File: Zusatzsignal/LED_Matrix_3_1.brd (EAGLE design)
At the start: 15.8 x 21.6 mm, 61 parts, among them IC1 PIC6C595D, X1 SSW-106-02-S-S

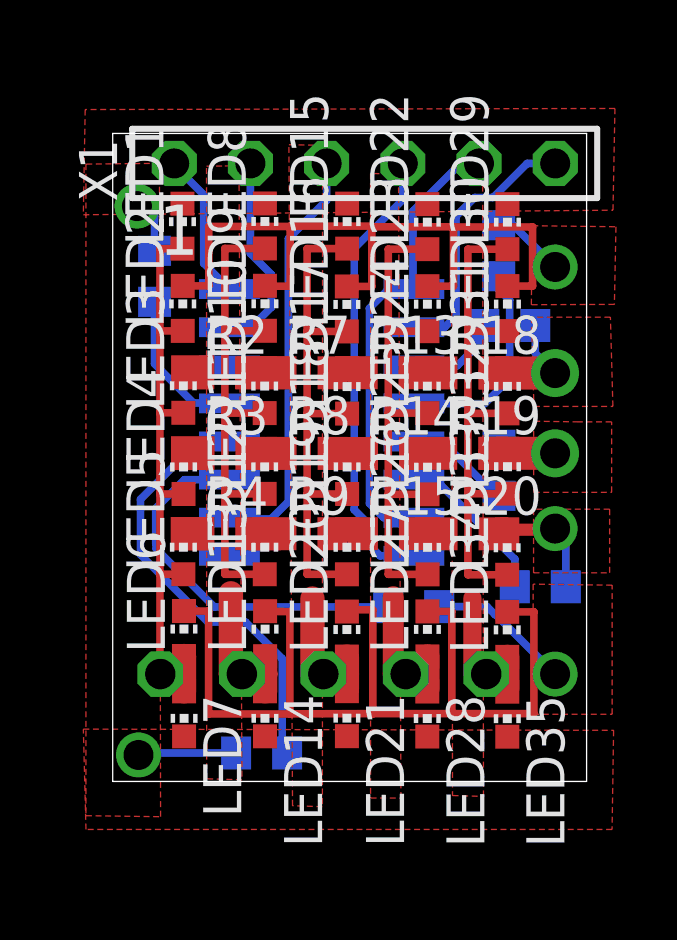
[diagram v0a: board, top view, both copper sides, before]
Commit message: Verbesserung der Zusatzanzeigerplatine
- Änderung des Layouts der Rückseite
- Änderung der Durchführungen auf RM
- Beseitigung von DRC-Fehlern
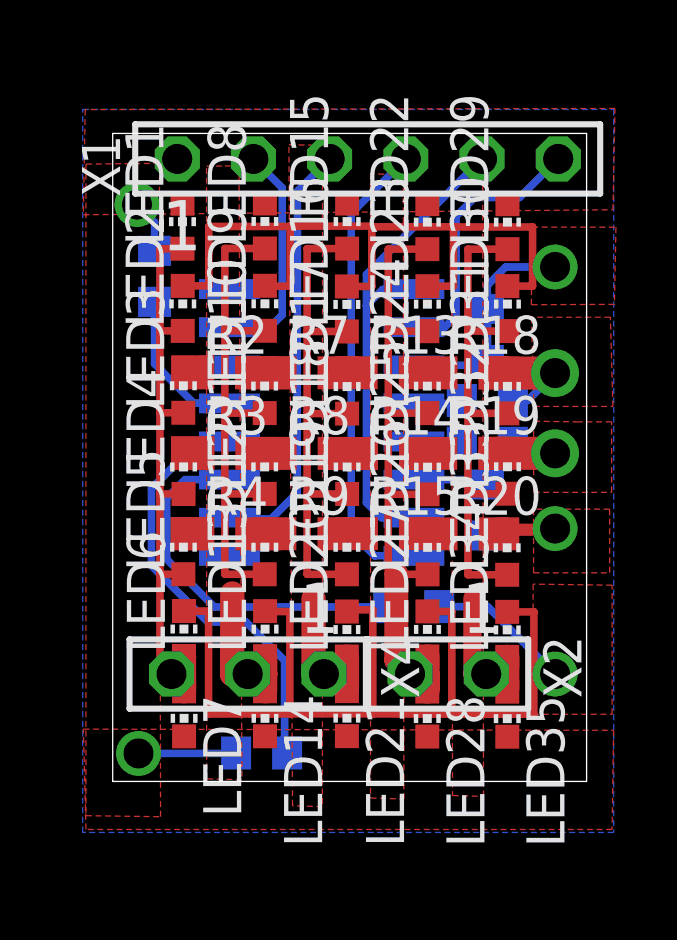
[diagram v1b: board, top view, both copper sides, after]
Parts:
- removed S1, S2, S3, S4, S5: (no value), pinhead:1X01
- added X2: SSW-102-02-S-S, con-samtec:SSW-102-02-S-S
- added X4: SSW-103-02-S-S, con-samtec:SSW-103-02-S-S
- R1, R10, R11, R12, R16, R5, R6: device eagle-ltspice:R0603 -> resistor:R0603
- moved R11 3.11 mm to (12.5, 9.05), turned to 90 degrees
- moved R5 2.81 mm to (12.5, 14.9)
- moved R6 2.61 mm to (12.5, 12.7)
- moved R10 0.98 mm to (12.5, 11.3), turned to 0 degrees
- moved X1 0.18 mm to (8.50, 20.8)
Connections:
- net N$4: now also R6.2; no longer R5.2
- net N$5: now also R5.2; no longer R6.2
- net S1: now also X4.3; no longer S1.1
- net S2: now also X4.2; no longer S2.1
- net S3: now also X4.1; no longer S3.1
- net S4: now also X2.2; no longer S4.1
- net S5: now also X2.1; no longer S5.1
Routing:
- net N$4: track 7.11 -> 1.65 mm
- net GND: track 4.95 -> 0.00 mm
- net N$6: track 5.39 -> 2.56 mm
- net N$7: track 3.59 -> 1.64 mm
- net SCK: track 6.10 -> 7.53 mm
- net VCC: track 15.4 -> 16.8 mm
- net S4: track 22.8 -> 23.7 mm
- net N$5: track 3.16 -> 4.08 mm
- net Z2: track 27.5 -> 28.3 mm
- net Z5: track 3.91 -> 4.44 mm
- added copper zone on layer 16, net GND

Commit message: Optimierung der Zusatzanzeiger & Hauptsignalplatine
- Symmetrischere Auslegung
- Entfernen von MISO/MISO connection zwischen Zusatzanzeiger und Hauptsignalschirm!
-> Zusatzanzeiger-MISO auf Signalschirmplatine nicht mehr connected (NC)
->mögliches Auslesen des DCC-Signals über den MISO-Anschluss (MOSI und SCK für I2C)
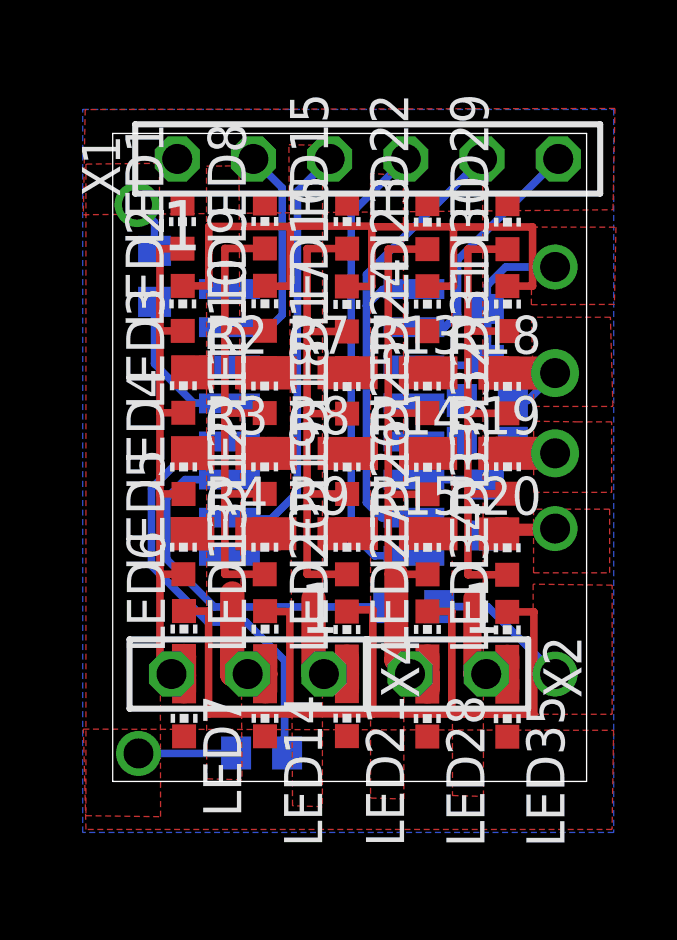
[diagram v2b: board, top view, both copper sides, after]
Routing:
- net DATA: track 9.08 -> 8.20 mm
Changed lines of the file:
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@@
 <layer number="14" name="Route14" color="1" fill="6" visible="no" active="yes"/>
 <layer number="15" name="Route15" color="4" fill="6" visible="no" active="yes"/>
-<layer number="16" name="Bottom" color="1" fill="1" visible="no" active="yes"/>
+<layer number="16" name="Bottom" color="1" fill="1" visible="yes" active="yes"/>
 <layer number="17" name="Pads" color="2" fill="1" visible="yes" active="yes"/>
 <layer number="18" name="Vias" color="2" fill="1" visible="yes" active="yes"/>
@@
 <layer number="20" name="Dimension" color="15" fill="1" visible="yes" active="yes"/>
 <layer number="21" name="tPlace" color="7" fill="1" visible="yes" active="yes"/>
-<layer number="22" name="bPlace" color="7" fill="1" visible="no" active="yes"/>
+<layer number="22" name="bPlace" color="7" fill="1" visible="yes" active="yes"/>
 <layer number="23" name="tOrigins" color="15" fill="1" visible="yes" active="yes"/>
-<layer number="24" name="bOrigins" color="15" fill="1" visible="no" active="yes"/>
+<layer number="24" name="bOrigins" color="15" fill="1" visible="yes" active="yes"/>
 <layer number="25" name="tNames" color="7" fill="1" visible="no" active="yes"/>
 <layer number="26" name="bNames" color="7" fill="1" visible="no" active="yes"/>
@@
 <layer number="38" name="bTest" color="7" fill="1" visible="no" active="yes"/>
 <layer number="39" name="tKeepout" color="4" fill="11" visible="yes" active="yes"/>
-<layer number="40" name="bKeepout" color="1" fill="11" visible="no" active="yes"/>
+<layer number="40" name="bKeepout" color="1" fill="11" visible="yes" active="yes"/>
 <layer number="41" name="tRestrict" color="4" fill="10" visible="yes" active="yes"/>
-<layer number="42" name="bRestrict" color="1" fill="10" visible="no" active="yes"/>
+<layer number="42" name="bRestrict" color="1" fill="10" visible="yes" active="yes"/>
 <layer number="43" name="vRestrict" color="2" fill="10" visible="yes" active="yes"/>
 <layer number="44" name="Drills" color="7" fill="1" visible="no" active="yes"/>
@@
 <layer number="50" name="dxf" color="7" fill="1" visible="no" active="no"/>
 <layer number="51" name="tDocu" color="7" fill="1" visible="yes" active="yes"/>
-<layer number="52" name="bDocu" color="7" fill="1" visible="no" active="yes"/>
+<layer number="52" name="bDocu" color="7" fill="1" visible="yes" active="yes"/>
 <layer number="53" name="tGND_GNDA" color="7" fill="9" visible="no" active="no"/>
 <layer number="54" name="bGND_GNDA" color="1" fill="9" visible="no" active="no"/>
@@
 <contactref element="X1" pad="6"/>
 <wire x1="10.03865" y1="15.1412375" x2="11.06430625" y2="15.1412375" width="0.254" layer="16"/>
-<wire x1="11.06430625" y1="15.1412375" x2="11.445471875" y2="15.522403125" width="0.254" layer="16"/>
-<wire x1="11.445471875" y1="15.522403125" x2="11.445471875" y2="18.8418375" width="0.254" layer="16"/>
-<wire x1="11.445471875" y1="18.8418375" x2="12.068634375" y2="19.465" width="0.254" layer="16"/>
-<wire x1="12.068634375" y1="19.465" x2="13.565" y2="19.465" width="0.254" layer="16"/>
-<wire x1="13.565" y1="19.465" x2="14.85" y2="20.75" width="0.254" layer="16"/>
+<wire x1="11.06430625" y1="15.1412375" x2="11.49594375" y2="15.56725625" width="0.254" layer="16"/>
+<wire x1="11.49594375" y1="15.56725625" x2="11.49594375" y2="17.390325" width="0.254" layer="16"/>
+<wire x1="11.49594375" y1="17.390325" x2="14.85" y2="20.75" width="0.254" layer="16"/>
 </signal>
 <signal name="N$1">
@@
 <signal name="N$3">
 <contactref element="R12" pad="2"/>
-<wire x1="9.17679375" y1="5.818303125" x2="3.385865625" y2="5.818303125" width="0.254" layer="16"/>
+<wire x1="3.385865625" y1="5.818303125" x2="9.17679375" y2="5.818303125" width="0.254" layer="16"/>
 <wire x1="9.17679375" y1="5.818303125" x2="9.18495" y2="5.826459375" width="0.254" layer="16"/>
 <contactref element="IC1" pad="11"/>
-<wire x1="3.89185" y1="10.0612375" x2="3.887965625" y2="10.057353125" width="0.254" layer="16"/>
+<wire x1="3.887965625" y1="10.057353125" x2="3.89185" y2="10.0612375" width="0.254" layer="16"/>
 <wire x1="3.385865625" y1="5.818303125" x2="1.8" y2="7.40416875" width="0.254" layer="16"/>
 <wire x1="1.8" y1="7.40416875" x2="1.8" y2="9.45" width="0.254" layer="16"/>

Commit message: Neuorganisation des Zusatzanzeigers
-> Werte begradigt und alle LEDs korrigiert
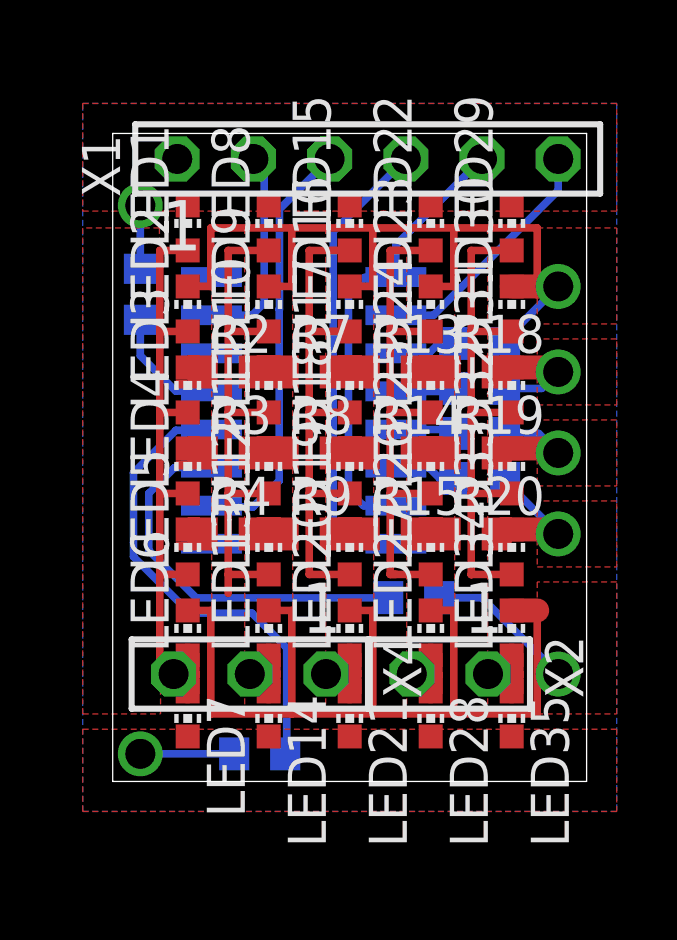
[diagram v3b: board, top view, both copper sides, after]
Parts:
- moved R11 1.09 mm to (12.2, 10.1), turned to 0 degrees
- moved R1 0.76 mm to (0.92, 16.2)
- moved IC1 0.72 mm to (6.37, 12.4)
- moved R6 0.48 mm to (12.2, 13.1)
- moved R10 0.42 mm to (12.2, 11.6)
- moved R5 0.39 mm to (12.2, 14.6), turned to 0 degrees
- moved R12 0.30 mm to (10.0, 6.13)
- moved LED1 0.18 mm to (2.50, 18.4)
- moved LED2 0.17 mm to (2.50, 15.8)
- moved LED34 0.16 mm to (13.3, 4.95)
- moved LED33 0.15 mm to (13.3, 7.65)
- moved LED29 0.15 mm to (13.3, 18.4)
- moved LED35 0.15 mm to (13.3, 2.25)
- moved LED3 0.15 mm to (2.50, 13.1)
- moved LED31 0.15 mm to (13.3, 13.1)
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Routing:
- net S4: track 23.7 -> 19.7 mm
- net S2: track 23.5 -> 20.2 mm
- net S3: track 22.8 -> 19.6 mm
- net S5: track 22.8 -> 19.7 mm
- net N$5: track 4.08 -> 2.08 mm
- net VCC: track 16.8 -> 15.4 mm
- net Z6: track 37.1 -> 38.5 mm
- net N$1: track 5.11 -> 4.06 mm
- net N$2: track 14.9 -> 15.9 mm
- net Z7: track 3.34 -> 4.03 mm
- net SCK: track 7.53 -> 6.88 mm
- net Z1: track 1.80 -> 2.36 mm
- net N$3: track 12.4 -> 13.0 mm
